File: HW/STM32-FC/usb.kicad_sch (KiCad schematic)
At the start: 33 parts, among them J2 USB_C_USB2.0_14P, J3 GH 1.25mm 6P, Q2 PMDPB30XN, Q3 PMDPB55XP, U2 USBLC6-2SC6, U3 TPS62840, U4 TPS62840, U5 TPS62840

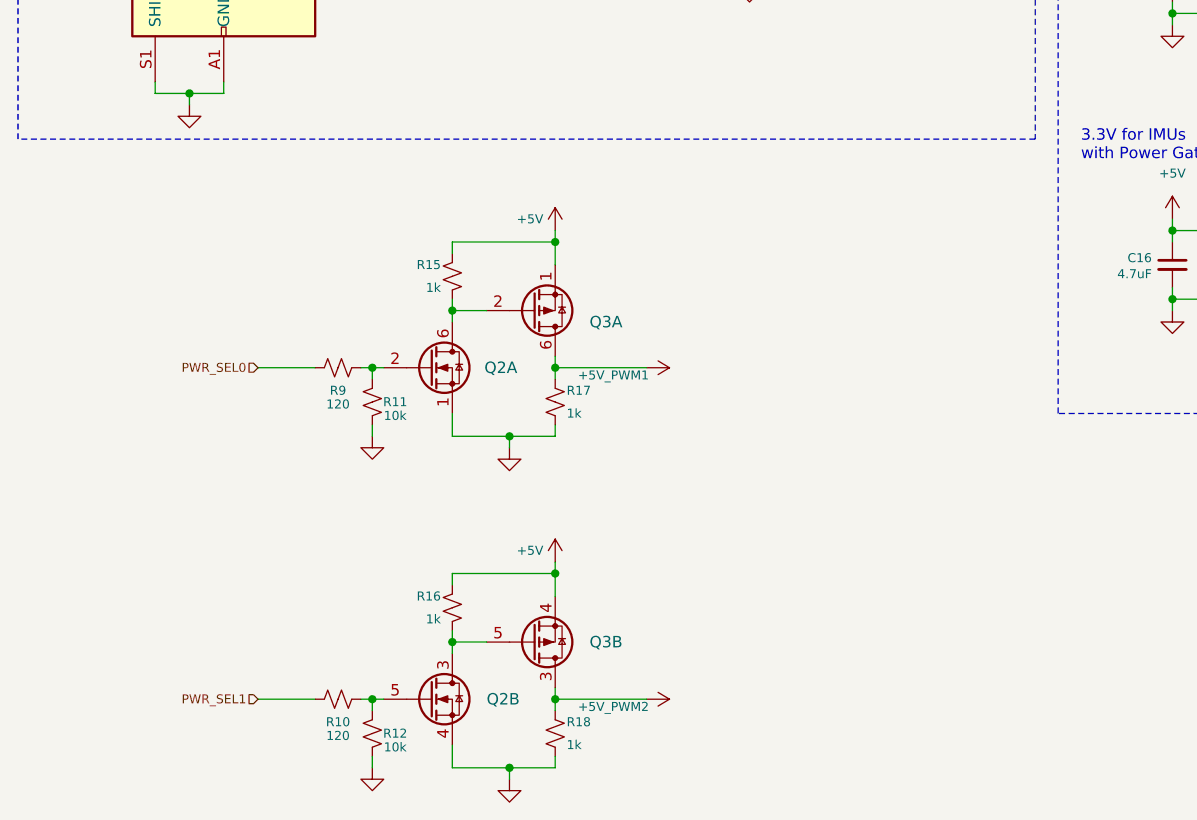
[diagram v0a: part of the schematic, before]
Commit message: HW Lib and RC code refactoring, GCS_log united and BMI323 IMU init.
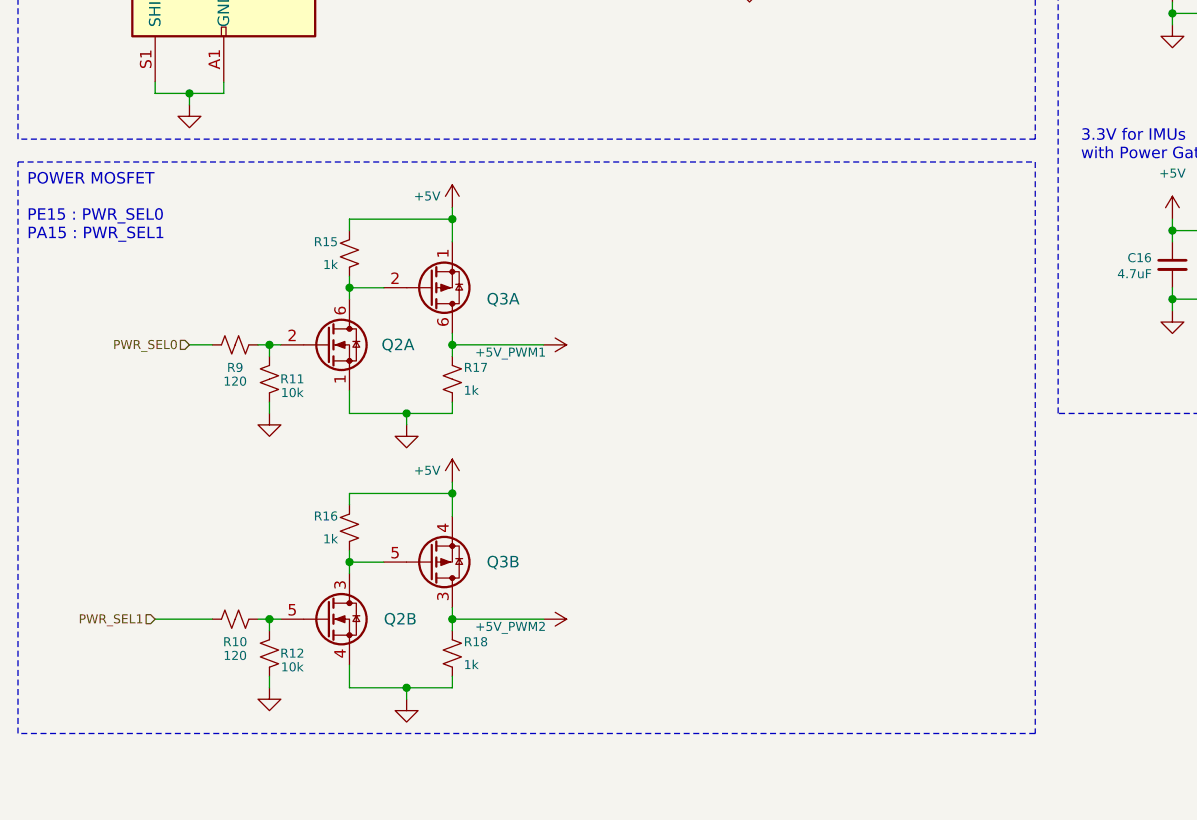
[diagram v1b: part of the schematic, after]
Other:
- note added: "PE15 : PWR_SEL0 PA15 : PWR_SEL1"
- note added: "POWER MOSFET"
- moved on the sheet: Q2A, Q2B, Q3A, Q3B, R10, R11, R12, R15, R16, R17, R18, R9
